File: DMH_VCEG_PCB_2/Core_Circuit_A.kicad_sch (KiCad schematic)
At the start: 104 parts, among them J21 Conn_01x10_PinHeader, J22 Conn_01x10_PinHeader, J24 Conn_01x06_PinHeader, Q1 BC558, Q10 BC548, Q2 BC558, Q3 BC548, Q4 BC548, Q5 MMBFJ113, Q6 MMBFJ113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

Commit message: Synced changes to PCB 2
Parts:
- removed Q5, Q6: MMBFJ113, Package_TO_SOT_THT:TO-92L_Inline, symbol Transistor_FET:MMBFJ113
- removed R11, R18, R19: 100k, Resistor_THT:R_Axial_DIN0207_L6.3mm_D2.5mm_P7.62mm_Horizontal, symbol Device:R_US
- added C73, C74: 100nF, Capacitor_THT:C_Rect_L7.0mm_W4.5mm_P5.00mm, symbol Device:C
- added Q5, Q6: BS170, Package_TO_SOT_THT:TO-92_Inline, symbol Transistor_FET:BS170
- added R195: 100R, Resistor_THT:R_Axial_DIN0207_L6.3mm_D2.5mm_P7.62mm_Horizontal, symbol Device:R_US
- added R196: 47k, Resistor_THT:R_Axial_DIN0207_L6.3mm_D2.5mm_P7.62mm_Horizontal, symbol Device:R_US
- added unit 4 of U3
- R32: value 100k -> 51k
- R34: value 100k -> 47k
- SW2: value DPDT_OnOn -> DPDT_OnOffOn; Function Long A -> Slow A
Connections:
- net -12V: no longer R41.1
- net GND: now also R44.1, SW2.2 (B), SW2.5 (B), C73.1, C74.1, R196.1; no longer C45.1, C50.2, R44.2, SW2.3 (C), SW2.6 (C)
- net InvGate: now also Q6.2 (G)
- net Max Level: now also R195.2; no longer U5.9 (-)
- net ProcGate: now also C46.1, D3.1 (K), D5.1 (K), J24.2 (Pin_2), R24.2, SW1.3 (C), U3.1, Q5.2 (G); no longer C48.2, D5.2 (A), R23.1, U1.1
- net at C45.2, C49.1, J21.6 (Pin_6)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: now also C74.2, Q5.1 (D), Q6.1 (D)
- net at U6.10: now also U6.6; no longer D16.2 (A)
- net at U6.9: now also U3.8; no longer U3.4
- net Inv Sus State: now reaches U6.2, U6.4
- net at C55.2, R46.1: now also U3.9; no longer U6.6
- net at C50.1, C51.1, J21.7 (Pin_7)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: now also C73.2
- net at R37.1, U1.8: now also U5.2 (-); no longer U5.3 (+)
- net at Q4.1 (C): now also Q6.3 (S)
- net at D15.2 (A), U5.1: now also R41.1
- net at R34.1, U1.14: now also D13.2 (A); no longer J24.3 (Pin_3), SW1.2 (B)
- net at C49.2: now also SW2.6 (C); no longer SW2.5 (B)
- net at Q2.1 (C): now also Q5.3 (S)
- net at C51.2: now also SW2.3 (C); no longer SW2.2 (B)
- net at SW2.4 (A): now also C45.1
- net at SW2.1 (A): now also C50.2
- net Sus State renamed Sus_State
- new net: R195.1, R196.2, U5.9 (-)
- new net: C48.2, D5.2 (A), R23.1, U1.1
- new net: R41.2, R44.2, U5.3 (+)
- new net: D16.2 (A), U3.4
- new net: D13.1 (K), J24.3 (Pin_3), SW1.2 (B)
- no-connect marks 5 -> 3
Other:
- moved on the sheet: C45, C49, C50, C51, C53, C55, C56, D13, D15, D16, J22J, J24B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

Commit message: PCB 2 comp placement ongoing
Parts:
- C73, C74: footprint Capacitor_THT:C_Rect_L7.0mm_W4.5mm_P5.00mm -> Capacitor_THT:C_Disc_D4.3mm_W1.9mm_P5.00mm
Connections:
- net at C45.1: now also SW2.6 (C); no longer SW2.4 (A)
- net at C50.2: now also SW2.3 (C); no longer SW2.1 (A)
- net at C49.2: now also SW2.4 (A); no longer SW2.6 (C)
- net at C51.2: now also SW2.1 (A); no longer SW2.3 (C)
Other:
- moved on the sheet: C45, C49, C50, C51
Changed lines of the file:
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@@
 	(symbol
 		(lib_id "Device:C")
-		(at 246.38 87.63 270)
+		(at 246.38 97.79 270)
 		(mirror x)
 		(unit 1)
@@
 		(dnp no)
 		(property "Reference" "C45"
-			(at 246.253 81.026 90)
+			(at 246.253 91.186 90)
 			(effects
 				(font
@@
 		)
 		(property "Value" "1uF"
-			(at 246.253 83.566 90)
+			(at 246.253 93.726 90)
 			(effects
 				(font
@@
 		)
 		(property "Footprint" "Capacitor_THT:C_Rect_L7.0mm_W4.5mm_P5.00mm"
-			(at 242.57 86.6648 0)
+			(at 242.57 96.8248 0)
 			(effects
 				(font
@@
 		)
 		(property "Datasheet" "~"
-			(at 246.38 87.63 0)
+			(at 246.38 97.79 0)
 			(effects
 				(font
@@
 		)
 		(property "Description" "Unpolarized capacitor"
-			(at 246.38 87.63 0)
+			(at 246.38 97.79 0)
 			(effects
 				(font
@@
 		)
 		(property "Function" ""
-			(at 246.38 87.63 0)
+			(at 246.38 97.79 0)
 			(effects
 				(font
@@
 		)
 		(instances
-			(project "DMH_VCEG_PCB_1"
+			(project "DMH_VCEG_PCB_2"
 				(path "/58f4306d-5387-4983-bb08-41a2313fd315/cb21e49a-1eb5-49c3-bf16-2a24a7e3f94c"
 					(reference "C45")
@@
 		(exclude_from_sim no)
 		(in_bom yes)
-		(on_board yes)
+		(on_board no)
 		(dnp no)
 		(property "Reference" "R196"
@@
 			)
 		)
-		(property "Footprint" "Capacitor_THT:C_Rect_L7.0mm_W4.5mm_P5.00mm"
+		(property "Footprint" "Capacitor_THT:C_Disc_D4.3mm_W1.9mm_P5.00mm"
 			(at 242.57 76.5048 0)
 			(effects
@@
 	(symbol
 		(lib_id "Device:C")
-		(at 260.35 115.57 90)
+		(at 260.35 125.73 90)
 		(unit 1)
 		(exclude_from_sim no)
@@
 		(dnp no)
 		(property "Reference" "C50"
-			(at 260.35 108.966 90)
+			(at 260.35 119.126 90)
 			(effects
 				(font
@@
 		)
 		(property "Value" "1uF"
-			(at 260.35 111.506 90)
+			(at 260.35 121.666 90)
 			(effects
 				(font
@@
 		)
 		(property "Footprint" "Capacitor_THT:C_Rect_L7.0mm_W4.5mm_P5.00mm"
-			(at 264.16 114.6048 0)
+			(at 264.16 124.7648 0)
 			(effects
 				(font
@@
 		)
 		(property "Datasheet" "~"
-			(at 260.35 115.57 0)
+			(at 260.35 125.73 0)
 			(effects
 				(font
@@
 		)
 		(property "Description" "Unpolarized capacitor"
-			(at 260.35 115.57 0)
+			(at 260.35 125.73 0)
 			(effects
 				(font
@@
 		)
 		(property "Function" "Main Cap A"
-			(at 267.716 117.094 90)
+			(at 267.716 127.254 90)
 			(effects
 				(font
@@
 		)
 		(instances
-			(project "DMH_VCEG_PCB_1"
+			(project "DMH_VCEG_PCB_2"
 				(path "/58f4306d-5387-4983-bb08-41a2313fd315/cb21e49a-1eb5-49c3-bf16-2a24a7e3f94c"
 					(reference "C50")
@@
 	(symbol
 		(lib_id "Device:C_Polarized")
-		(at 246.38 97.79 90)
+		(at 246.38 87.63 90)
 		(unit 1)
 		(exclude_from_sim no)
@@
 		(dnp no)
 		(property "Reference" "C49"
-			(at 245.618 91.186 90)
+			(at 245.618 81.026 90)
 			(effects
 				(font
@@
 		)
 		(property "Value" "10uF"
-			(at 245.618 93.726 90)
+			(at 245.618 83.566 90)
 			(effects
 				(font
@@
 		)
 		(property "Footprint" "Capacitor_THT:CP_Radial_D4.0mm_P1.50mm"
-			(at 250.19 96.8248 0)
+			(at 250.19 86.6648 0)
 			(effects
 				(font
@@
 		)
 		(property "Datasheet" "~"
-			(at 246.38 97.79 0)
+			(at 246.38 87.63 0)
 			(effects
 				(font
@@
 		)
 		(property "Description" "Polarized capacitor"
-			(at 246.38 97.79 0)
+			(at 246.38 87.63 0)
 			(effects
 				(font
@@
 		)
 		(property "Function" ""
-			(at 246.38 97.79 0)
+			(at 246.38 87.63 0)
 			(effects
 				(font
@@
 		)
 		(instances
-			(project "DMH_VCEG_PCB_1"
+			(project "DMH_VCEG_PCB_2"
 				(path "/58f4306d-5387-4983-bb08-41a2313fd315/cb21e49a-1eb5-49c3-bf16-2a24a7e3f94c"
 					(reference "C49")
@@
 			)
 		)
-		(property "Footprint" "Capacitor_THT:C_Rect_L7.0mm_W4.5mm_P5.00mm"
+		(property "Footprint" "Capacitor_THT:C_Disc_D4.3mm_W1.9mm_P5.00mm"
 			(at 256.54 104.4448 0)
 			(effects
@@
 	(symbol
 		(lib_id "Device:C_Polarized")
-		(at 260.35 125.73 90)
+		(at 260.35 115.57 90)
 		(unit 1)
 		(exclude_from_sim no)
@@
 		(dnp no)
 		(property "Reference" "C51"
-			(at 260.35 119.126 90)
+			(at 260.35 108.966 90)
 			(effects
 				(font
@@
 		)
 		(property "Value" "10uF"
-			(at 260.35 121.666 90)
+			(at 260.35 111.506 90)
 			(effects
 				(font
@@
 		)
 		(property "Footprint" "Capacitor_THT:CP_Radial_D4.0mm_P1.50mm"
-			(at 264.16 124.7648 0)
+			(at 264.16 114.6048 0)
 			(effects
 				(font
@@
 		)
 		(property "Datasheet" "~"
-			(at 260.35 125.73 0)
+			(at 260.35 115.57 0)
 			(effects
 				(font
@@
 		)
 		(property "Description" "Polarized capacitor"
-			(at 260.35 125.73 0)
+			(at 260.35 115.57 0)
 			(effects
 				(font
@@
 		)
 		(property "Function" ""
-			(at 260.35 125.73 0)
+			(at 260.35 115.57 0)
 			(effects
 				(font
@@
 		)
 		(instances
-			(project "DMH_VCEG_PCB_1"
+			(project "DMH_VCEG_PCB_2"
 				(path "/58f4306d-5387-4983-bb08-41a2313fd315/cb21e49a-1eb5-49c3-bf16-2a24a7e3f94c"
 					(reference "C51")
@@
 		(exclude_from_sim no)
 		(in_bom yes)
-		(on_board yes)
+		(on_board no)
 		(dnp no)
 		(property "Reference" "R195"

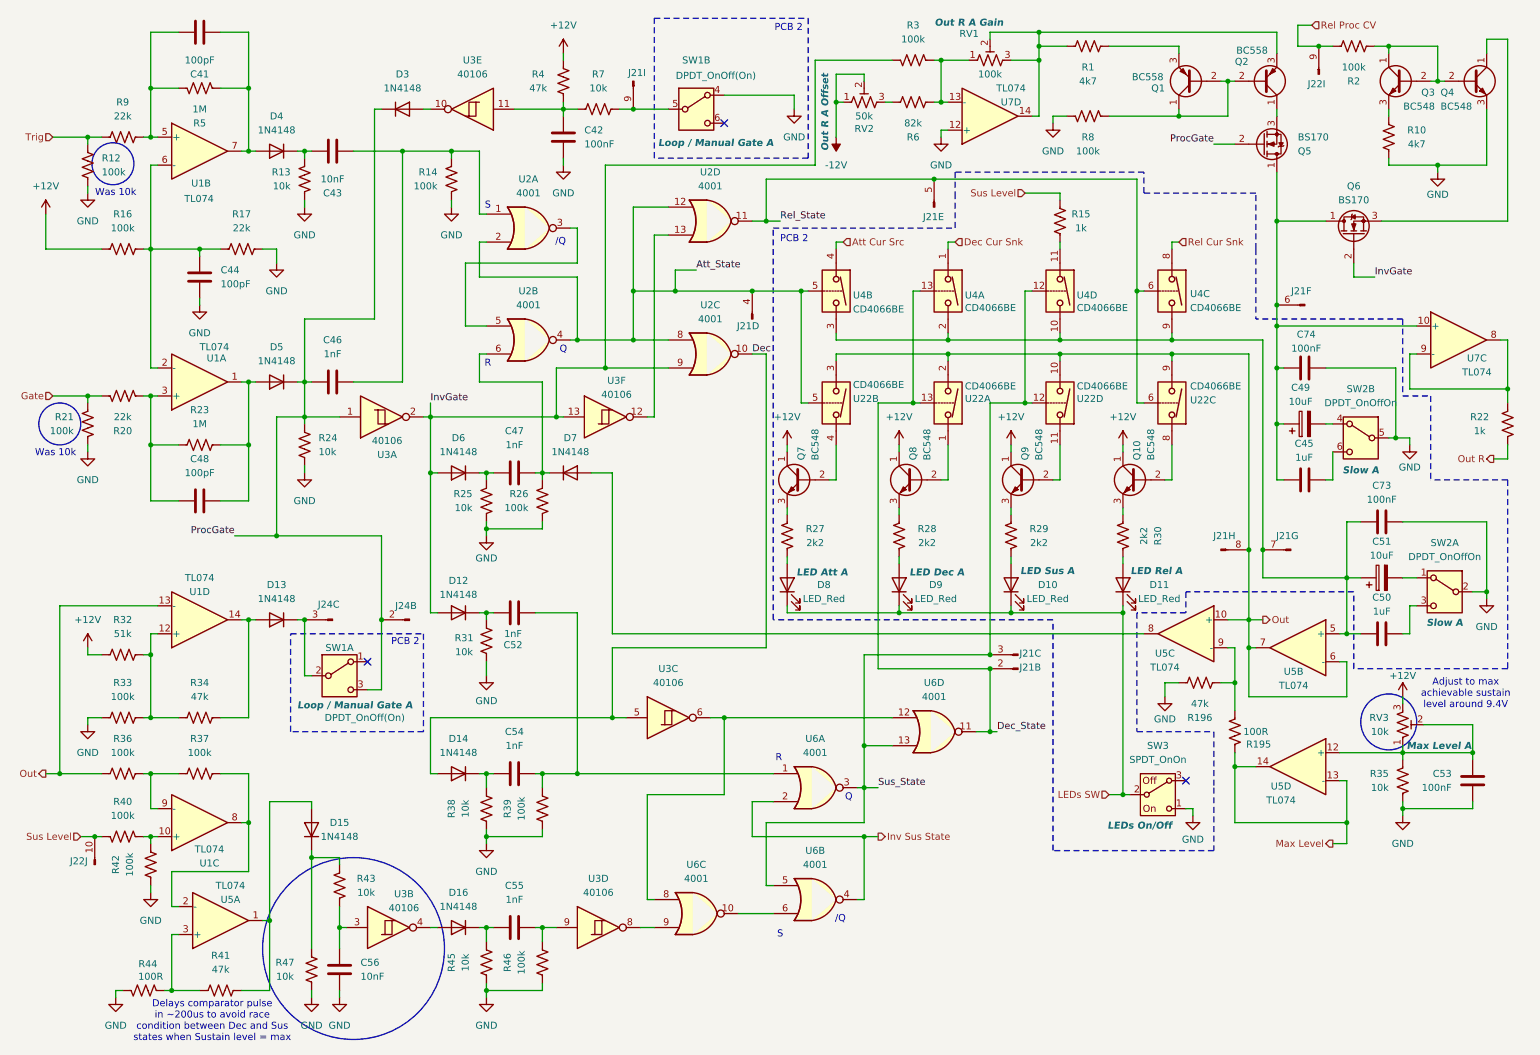
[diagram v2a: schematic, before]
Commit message: Synced PCB 1 and 2
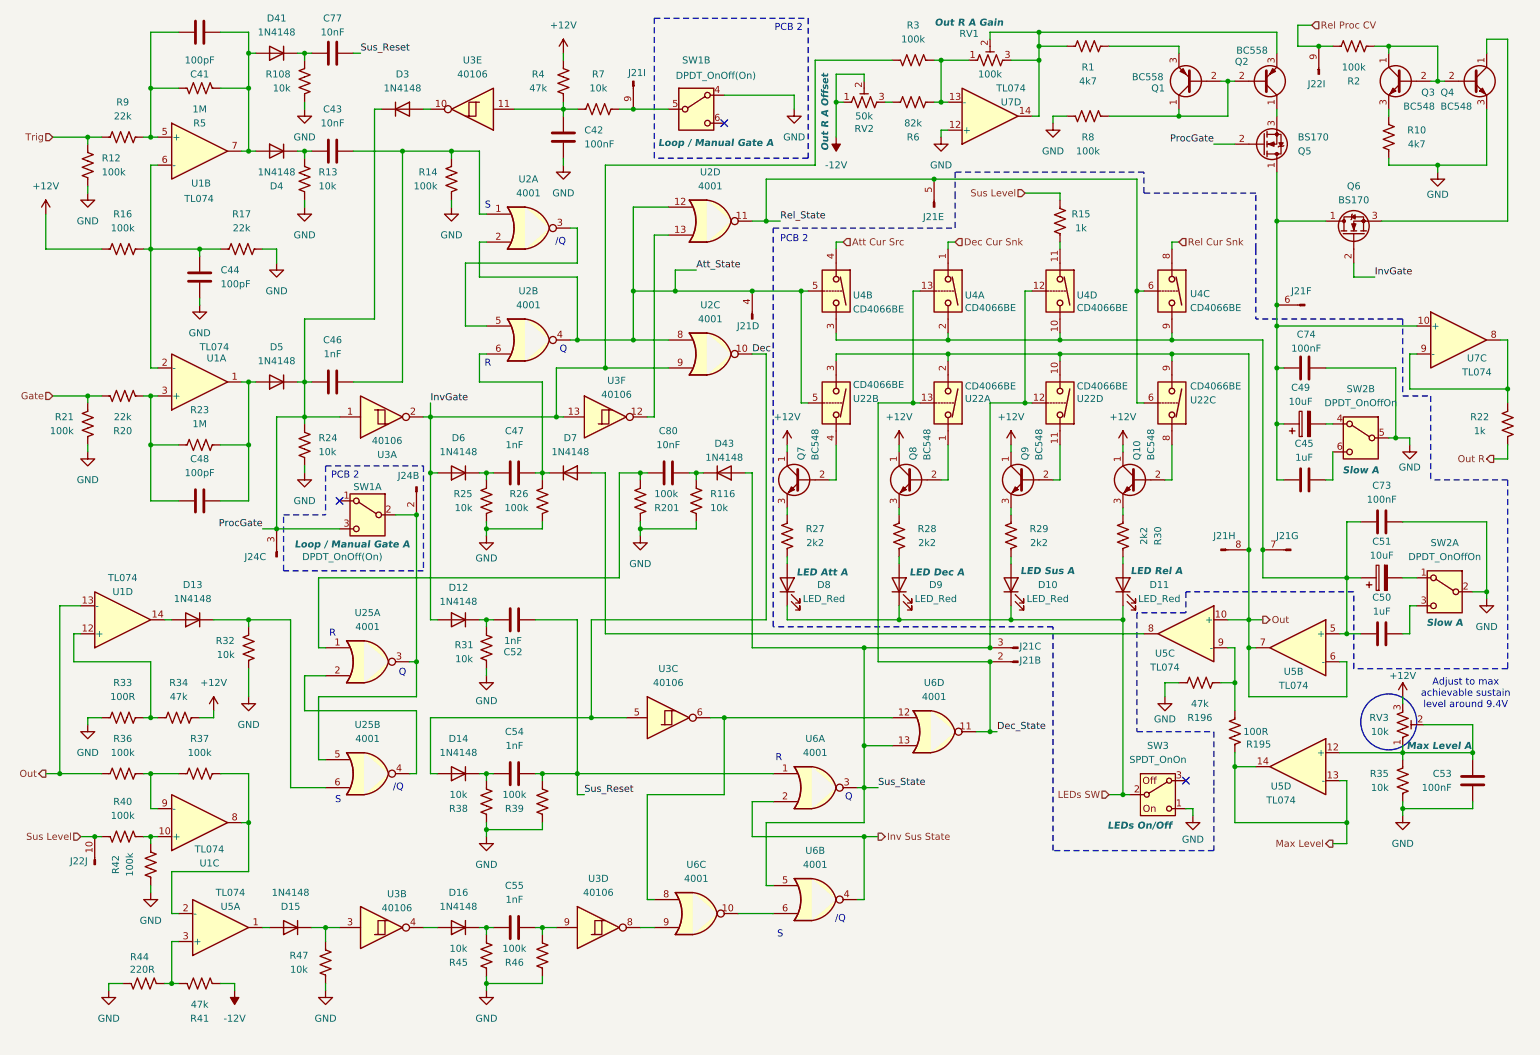
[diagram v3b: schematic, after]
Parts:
- removed C56: 10nF, Capacitor_THT:C_Disc_D4.3mm_W1.9mm_P5.00mm, symbol Device:C
- removed R43: 10k, Resistor_THT:R_Axial_DIN0207_L6.3mm_D2.5mm_P7.62mm_Horizontal, symbol Device:R_US
- added C77, C80: 10nF, Capacitor_THT:C_Disc_D4.3mm_W1.9mm_P5.00mm, symbol Device:C
- added D41, D43: 1N4148, Diode_THT:D_DO-35_SOD27_P7.62mm_Horizontal, symbol Diode:1N4148
- added R108, R116: 10k, Resistor_THT:R_Axial_DIN0207_L6.3mm_D2.5mm_P7.62mm_Horizontal, symbol Device:R_US
- added R201: 100k, Resistor_THT:R_Axial_DIN0207_L6.3mm_D2.5mm_P7.62mm_Horizontal, symbol Device:R_US
- added U25: 4001, Package_DIP:DIP-14_W7.62mm_Socket, symbol 4xxx:4001
- R32: value 51k -> 10k
- R33: value 100k -> 100R
- R44: value 100R -> 220R
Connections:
- net +12V: now also R34.1; no longer R32.2
- net -12V: now also R41.1
- net GND: now also R32.1, R108.1, R116.1, R201.2
- net ProcGate: now also J24.3 (Pin_3); no longer J24.2 (Pin_2)
- net Sus_State: now also D43.2 (A)
- net Sus_Reset: now reaches C52.2, C54.2, R39.1, U6.1
- net Sus_Reset: now also C77.2
- net at U3.3: now also D15.1 (K), R47.1
- net at R33.1, R34.2, U1.12 (+): no longer R32.1
- net at D15.2 (A), U5.1: no longer R41.1
- net at D13.2 (A), U1.14: no longer R34.1
- net at C41.2, D4.2 (A), R5.1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: now also D41.2 (A)
- new net: J24.2 (Pin_2), SW1.2 (B), U25.3, U25.5
- new net: C77.1, D41.1 (K), R108.2
- new net: C80.1, R201.1, U25.1
- new net: U25.2, U25.4
- new net: D13.1 (K), R32.2, U25.6
- new net: C80.2, D43.1 (K), R116.2
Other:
- note removed: "Delays comparator pulse in ~200us to avoid race condition between Dec and Sus states when Sustain level = max"
- note removed: "Was 10k"
- moved on the sheet: C52, D12, D13, D15, D4, J21B, J21C, R13, R31, R34, R38, R39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

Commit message: Restarted component placing on Main
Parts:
- renumbered J21 to J22, J21 to J23
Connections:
- net Att_State: now also J21.8 (Pin_8); no longer J21.4 (Pin_4)
- net Dec_State: now also J21.4 (Pin_4); no longer J21.2 (Pin_2)
- net Out: now also J22.6 (Pin_6); no longer J22.8 (Pin_8)
- net ProcGate: now also J24.2 (Pin_2); no longer J24.3 (Pin_3)
- net Rel_State: now also J21.9 (Pin_9); no longer J21.5 (Pin_5)
- net Sus_State: now also J21.5 (Pin_5); no longer J21.3 (Pin_3)
- net at C45.2, C49.1, C74.2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: now also J23.10 (Pin_10); no longer J23.6 (Pin_6)
- net at SW1.2 (B), U25.3, U25.5: now also J24.3 (Pin_3); no longer J24.2 (Pin_2)
- net at C50.1, C51.1, C73.2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: now also J21.6 (Pin_6); no longer J21.7 (Pin_7)

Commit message: PCB 2 placement done
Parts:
- D10, D11, D8, D9: value LED_Red -> LED_R
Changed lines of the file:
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@@
 			)
 		)
-		(property "Value" "LED_Red"
+		(property "Value" "LED_R"
 			(at 159.0675 119.38 90)
 			(effects
@@
 			)
 		)
-		(property "Value" "LED_Red"
+		(property "Value" "LED_R"
 			(at 179.3875 119.38 90)
 			(effects
@@
 			)
 		)
-		(property "Value" "LED_Red"
+		(property "Value" "LED_R"
 			(at 219.964 119.38 90)
 			(effects
@@
 			)
 		)
-		(property "Value" "LED_Red"
+		(property "Value" "LED_R"
 			(at 199.7075 119.38 90)
 			(effects

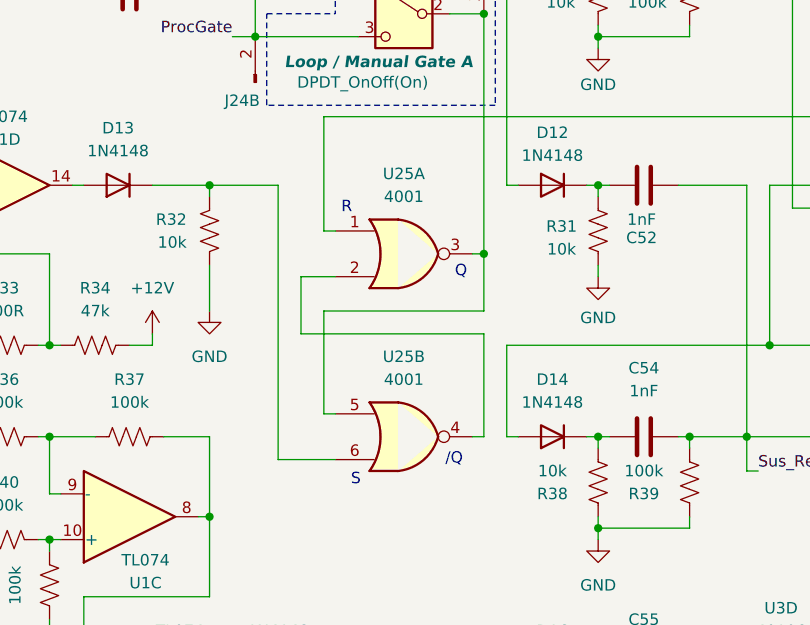
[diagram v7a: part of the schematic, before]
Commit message: PCB 1 placement in progress
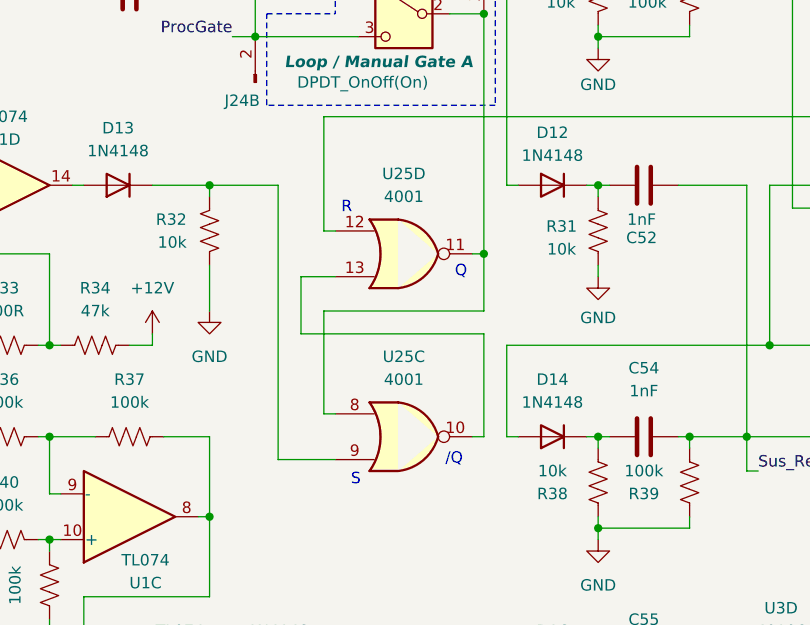
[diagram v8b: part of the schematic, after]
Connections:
- net at J24.3 (Pin_3), SW1.2 (B): now also U25.11, U25.8; no longer U25.3, U25.5
- net at C80.1, R201.1: now also U25.12; no longer U25.1
- net at D13.1 (K), R32.2: now also U25.9; no longer U25.6
- new net: U25.10, U25.13
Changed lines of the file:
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@@
 		(lib_id "4xxx:4001")
 		(at 76.2 151.13 0)
-		(unit 2)
+		(unit 3)
 		(exclude_from_sim no)
 		(in_bom yes)
@@
 				(path "/58f4306d-5387-4983-bb08-41a2313fd315/cb21e49a-1eb5-49c3-bf16-2a24a7e3f94c"
 					(reference "U25")
-					(unit 2)
+					(unit 3)
 				)
 			)
@@
 		(lib_id "4xxx:4001")
 		(at 76.2 130.81 0)
-		(unit 1)
+		(unit 4)
 		(exclude_from_sim no)
 		(in_bom yes)
@@
 				(path "/58f4306d-5387-4983-bb08-41a2313fd315/cb21e49a-1eb5-49c3-bf16-2a24a7e3f94c"
 					(reference "U25")
-					(unit 1)
+					(unit 4)
 				)
 			)
